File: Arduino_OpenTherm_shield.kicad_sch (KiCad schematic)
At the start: 54 parts, among them J1 BOILER, J2 THERM, Q1 MMBT2907A, Q2 MMBT2907A, Q3 MMBT2907A, Q4 MMBT2907A, Q5 MMBT2222A, Q6 MMBT2222A, U1 TPS61040DBV, U2 LTV-817S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

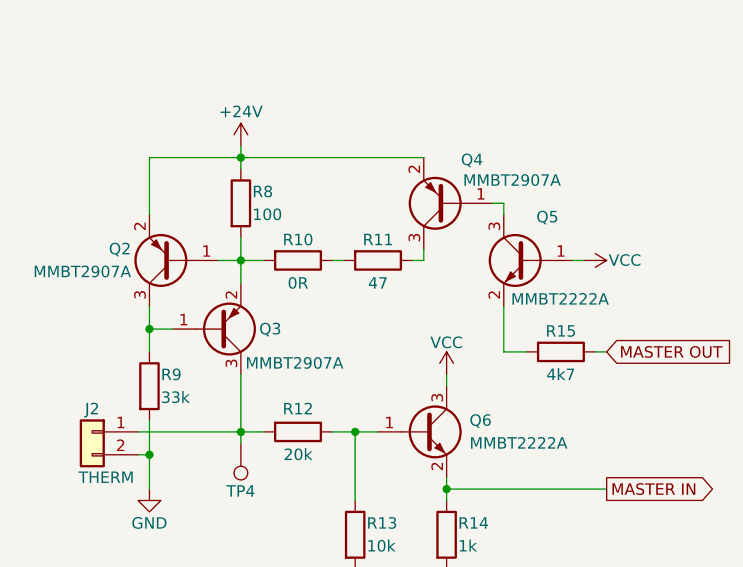
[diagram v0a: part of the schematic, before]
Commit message: Corrected value of the resistance responsible for the High state of the OT bus
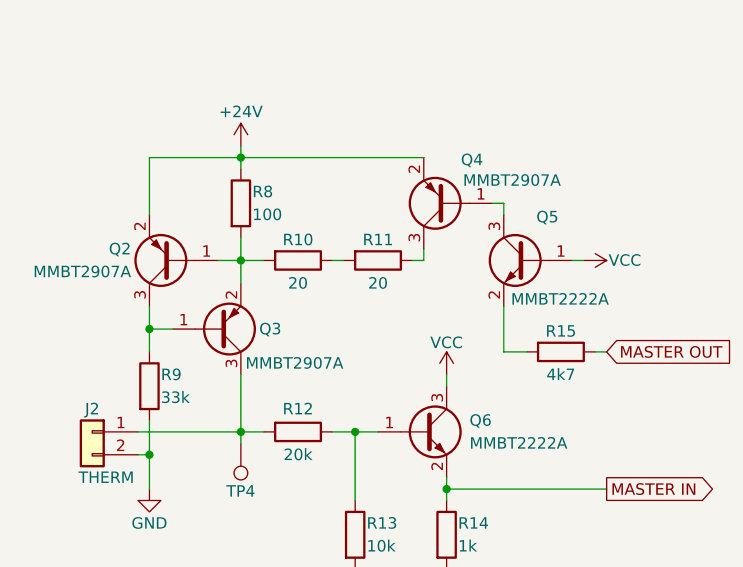
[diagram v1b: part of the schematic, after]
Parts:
- R10: value 0R -> 20; LCSC C21189 -> C22950
- R11: value 47 -> 20; LCSC C23182 -> C22950
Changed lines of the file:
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@@
 	(title_block
 		(title "OpenTherm Arduino Shield")
-		(date "2025-03-30")
+		(date "2025-04-16")
 		(rev "1.1")
 		(company "© 2025 MPro")
@@
 			)
 		)
-		(property "Value" "47"
+		(property "Value" "20"
 			(at 85.09 107.95 90)
 			(effects
@@
 			)
 		)
-		(property "LCSC" "C23182"
+		(property "LCSC" "C22950"
 			(at 85.09 105.41 90)
 			(effects
@@
 			)
 		)
-		(property "Value" "0R"
+		(property "Value" "20"
 			(at 76.2 107.95 90)
 			(effects
@@
 			)
 		)
-		(property "LCSC" "C21189"
+		(property "LCSC" "C22950"
 			(at 76.2 105.41 90)
 			(effects

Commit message: updated bom list
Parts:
- U1: value TPS61040DBV -> MT3540-F23; LCSC C7722 -> C181783
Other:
- note added: "Replacement: •(LCSC C370888) RY3750"
- note removed: "Replacements: •(LCSC C181783) MT3540-F23 •(LCSC C370888) RY3750"
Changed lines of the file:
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@@
 		(comment 4 "Licensed under CERN-OHL-P v2 or any later version")
 	)
-	(text "Replacements:\n•(LCSC C181783) MT3540-F23\n•(LCSC C370888) RY3750"
+	(text "Replacement:\n•(LCSC C370888) RY3750"
 		(exclude_from_sim no)
 		(at 77.216 187.96 0)
@@
 			)
 		)
-		(property "Value" "TPS61040DBV"
+		(property "Value" "MT3540-F23"
 			(at 89.662 183.134 0)
 			(effects
@@
 			)
 		)
-		(property "LCSC" "C7722"
+		(property "LCSC" "C181783"
 			(at 82.55 176.53 0)
 			(effects

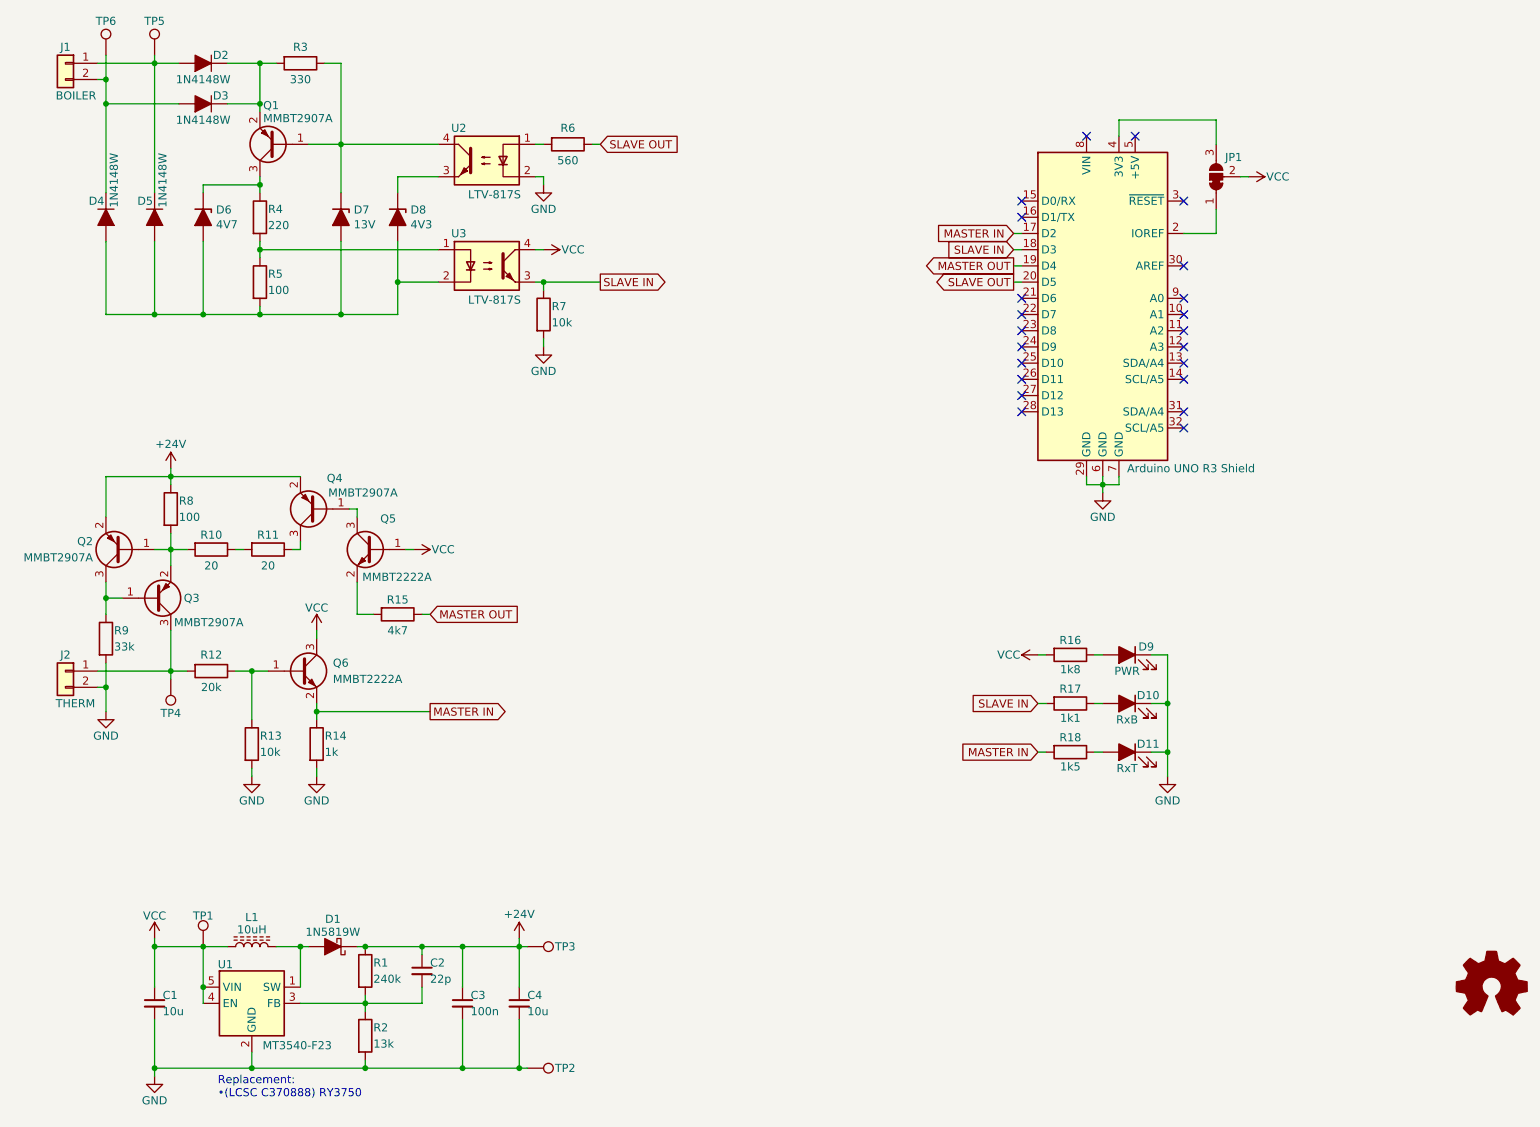
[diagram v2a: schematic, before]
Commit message: HW rev 1.2 [fixed translation of MASTER_IN signal logic levels]
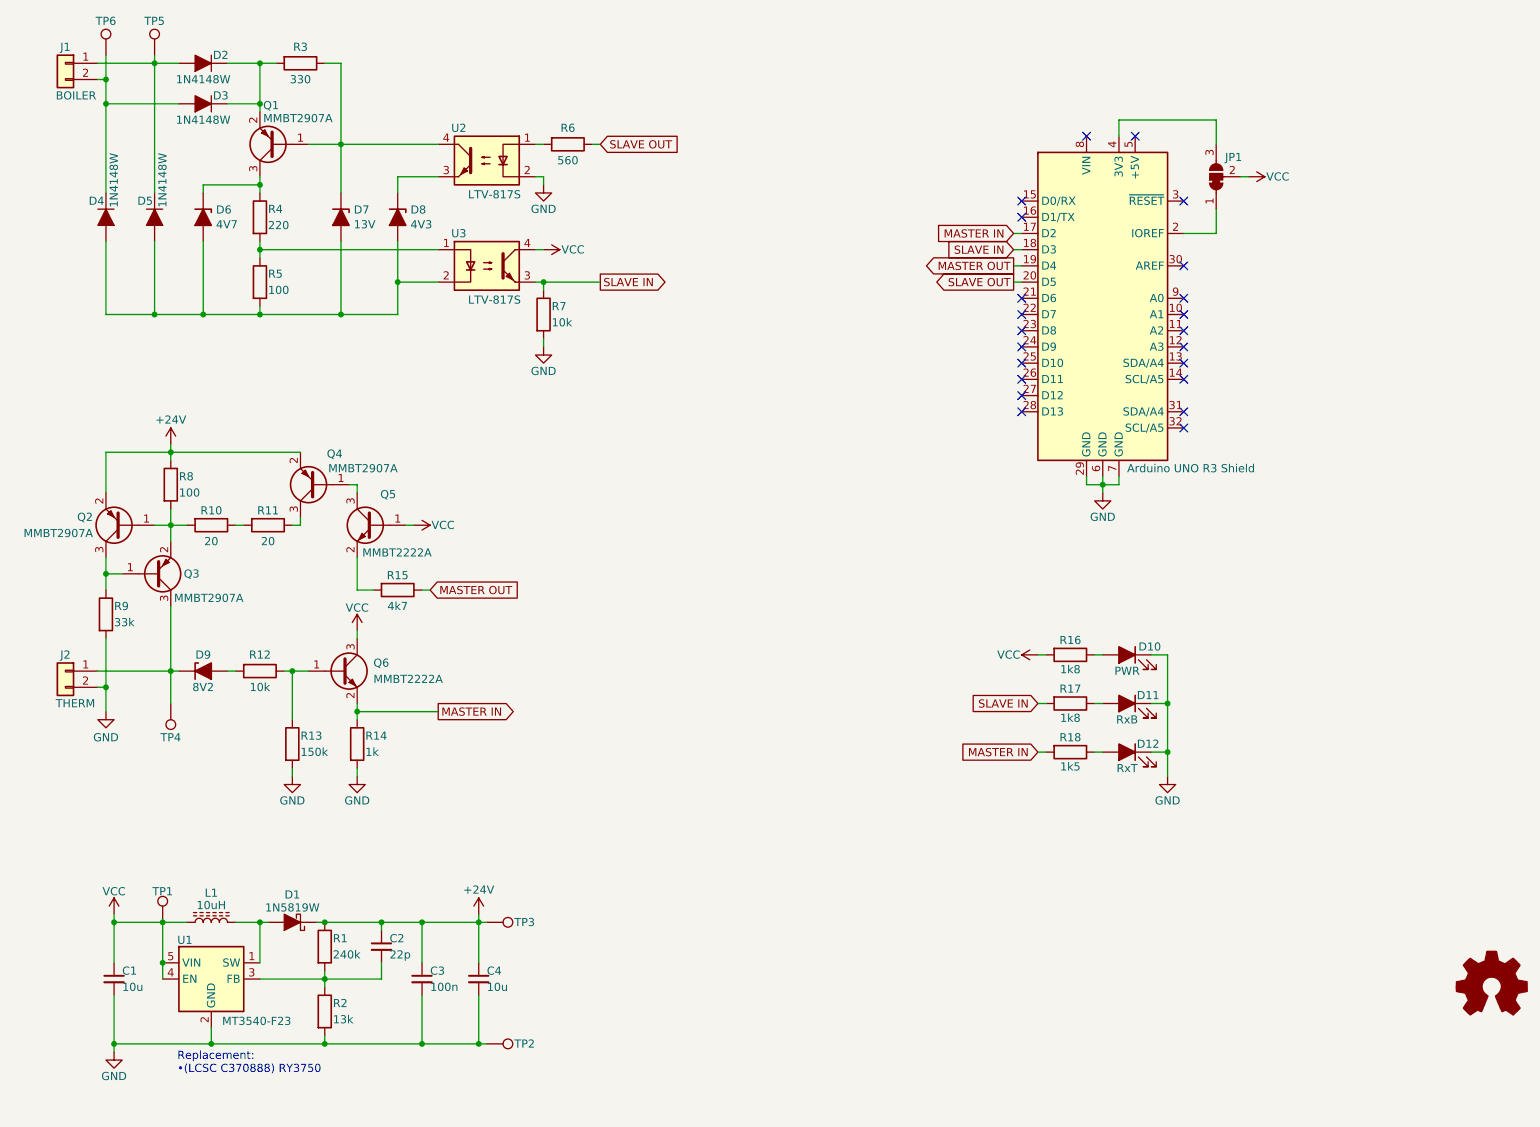
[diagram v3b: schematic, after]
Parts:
- added D9: 8V2, footprints:D_SOD-123, symbol archive:D_Zener_ALT-Device
- L1: LCSC C5349663 -> C177242
- R12: value 20k -> 10k; LCSC C4184 -> C25804
- R13: value 10k -> 150k; LCSC C25804 -> C22807
- R17: value 1k1 -> 1k8; LCSC C22764 -> C4177
- U2, U3: LCSC C108319 -> C109227
- renumbered D9 to D10, D10 to D11, D11 to D12
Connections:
- net at J2.1 (Pin_1), Q3.3 (C), TP4.1: now also D9.1 (K); no longer R12.2
- new net: D9.2 (A), R12.2
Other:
- moved on the sheet: C1, C2, C3, C4, D1, L1, Q2, Q3, Q4, Q5, Q6, R1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

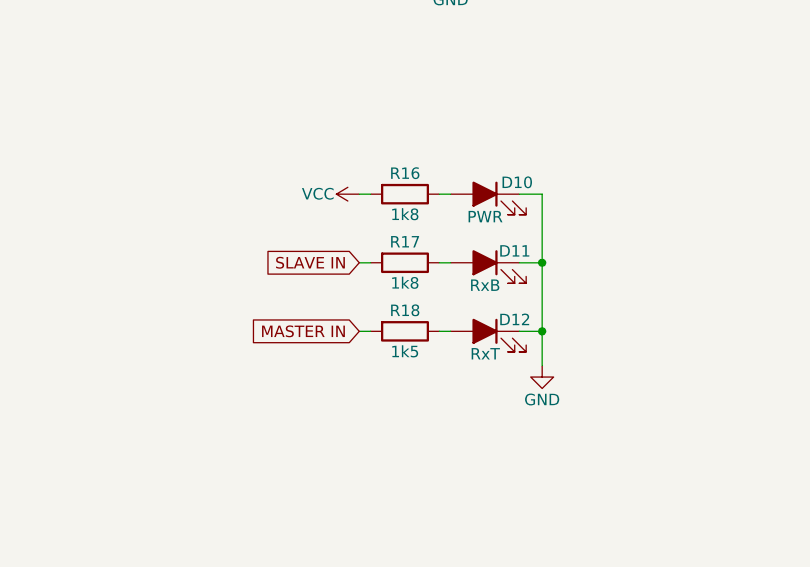
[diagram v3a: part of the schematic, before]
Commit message: RxB LED brightness adjusted
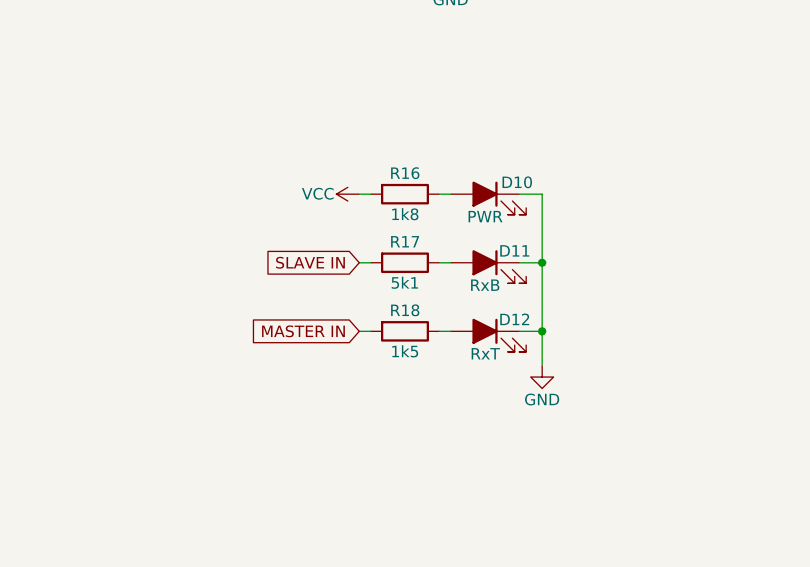
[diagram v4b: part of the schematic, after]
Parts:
- R17: value 1k8 -> 5k1; LCSC C4177 -> C23186
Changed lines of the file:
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@@
 	(title_block
 		(title "OpenTherm Arduino Shield")
-		(date "2025-07-11")
+		(date "2025-09-14")
 		(rev "1.2")
 		(company "© 2025 MPro")
@@
 			)
 		)
-		(property "Value" "1k8"
+		(property "Value" "5k1"
 			(at 210.82 131.826 90)
 			(effects
@@
 			)
 		)
-		(property "LCSC" "C4177"
+		(property "LCSC" "C23186"
 			(at 210.82 129.54 90)
 			(effects
